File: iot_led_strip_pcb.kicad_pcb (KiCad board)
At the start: 2 copper layers, 50 x 50 mm, 57 parts, among them J1 I2C Expansion, J2 Conn_01x03_Socket, J3 GT-USB-7010ASV, J4 Barrel_Jack_Switch_Pin3Ring, J5 TC2050-IDC_Cortex-M, J6 Conn_01x03_Socket_Solderwire, Q1 BSS138, SW1 RESET, SW2 FLASH, U1 AMS1117-3.3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

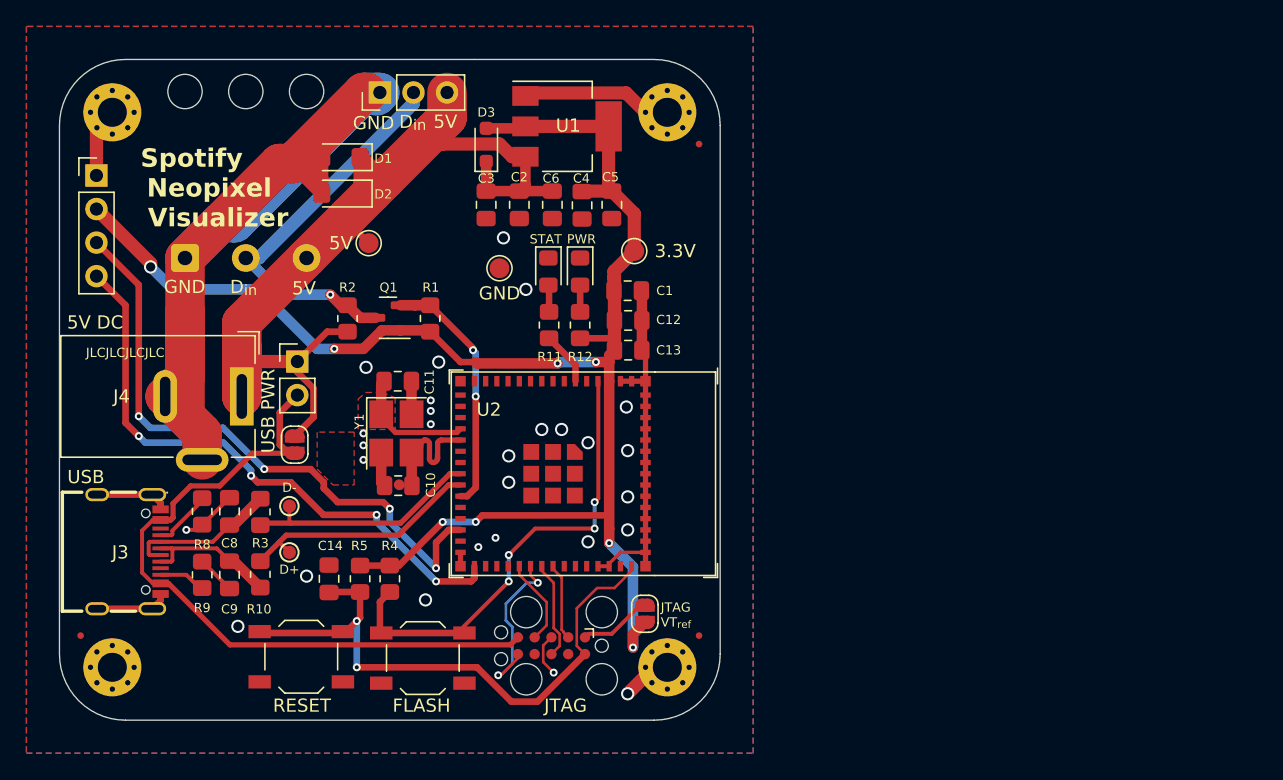
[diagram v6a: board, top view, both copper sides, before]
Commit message: modified sch to change over to esp32-s2-solo-2, should be much easier to solder
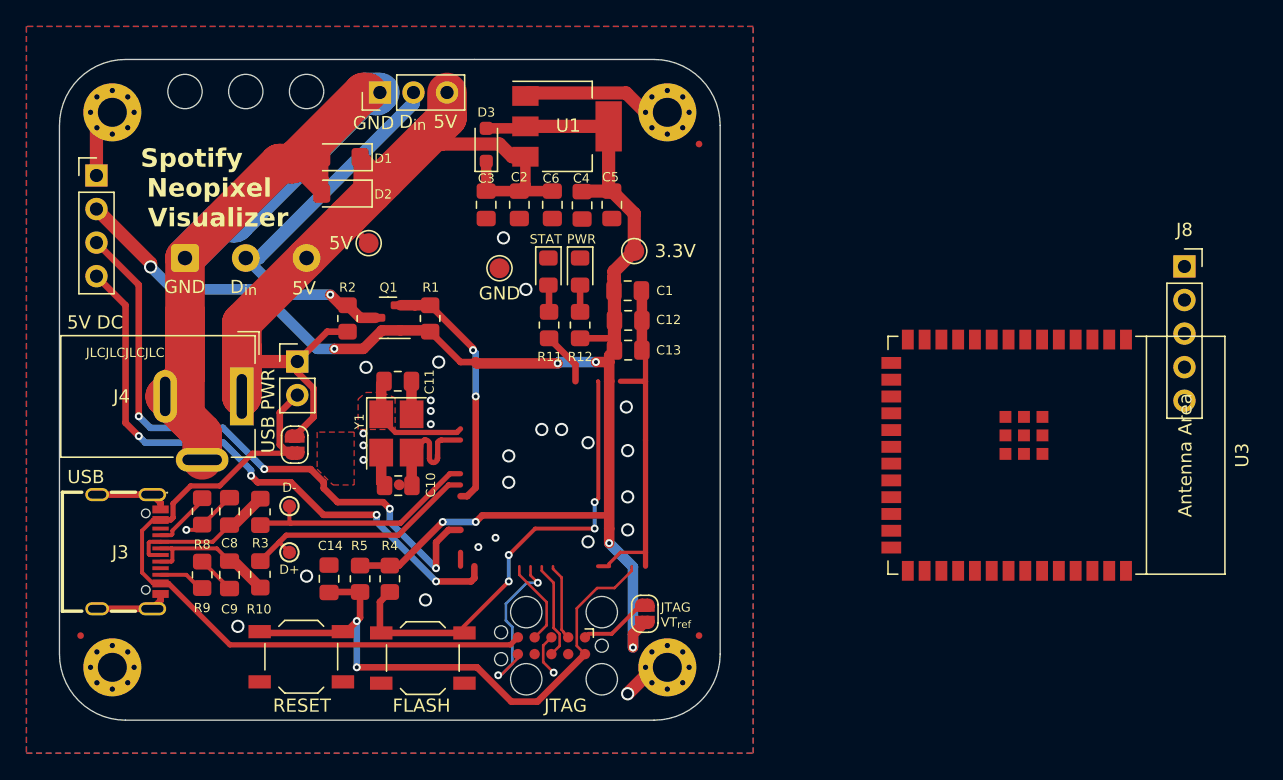
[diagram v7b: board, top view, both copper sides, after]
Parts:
- removed U2: ESP32-S2-MINI-1, PCM_Espressif:ESP32-S2-MINI-1
- added J8: UART, Connector_PinSocket_2.54mm:PinSocket_1x05_P2.54mm_Vertical, F.Cu at (195.1, 85.7)
- added U3: ESP32-S2-SOLO, Espressif:ESP32-S2-SOLO, F.Cu at (182.4, 100.0)
- Y1: value Crystal_32Mhz -> Crystal_32Khz

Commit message: board redesign around ESP32-S2-SOLO-2
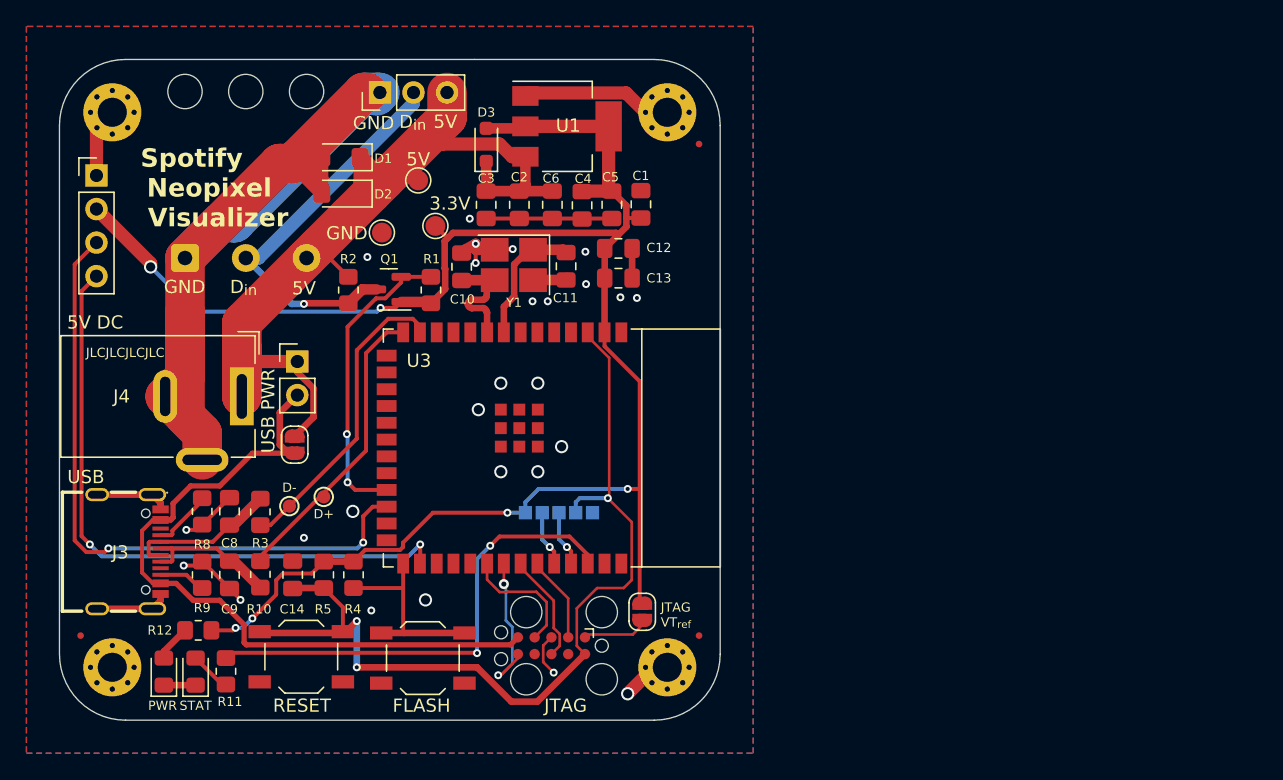
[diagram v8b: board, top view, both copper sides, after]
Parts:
- J8: footprint Connector_PinSocket_2.54mm:PinSocket_1x05_P2.54mm_Vertical -> footprint:5 Pin Pad array; moved to B.Cu
- moved J8 47.7 mm to (151.0, 103.6), turned to 180 degrees
- moved D5 43.7 mm to (117.9, 116.3), turned to 90 degrees
- moved D4 40.4 mm to (120.3, 116.3), turned to 90 degrees
- moved U3 38.2 mm to (144.3, 99.4)
- moved R12 37.0 mm to (120.5, 113.2), turned to 0 degrees
- moved R11 35.8 mm to (122.6, 116.3), turned to 90 degrees
- moved C10 17.2 mm to (140.4, 85.7), turned to 90 degrees
- moved Y1 15.5 mm to (144.4, 85.5), turned to 180 degrees
- moved C11 15.4 mm to (148.3, 85.7), turned to -90 degrees
- moved TP2 15.2 mm to (138.4, 82.6)
- moved TP3 9.30 mm to (134.4, 83.1)
- moved C1 6.61 mm to (154.0, 81.0), turned to 90 degrees
- moved TP1 6.05 mm to (137.2, 79.2)
- moved C12 5.50 mm to (152.3, 84.3)
- moved C13 5.50 mm to (152.3, 86.5)
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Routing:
- net Net-(U3-GPIO2/TOUCH2/ADC1_CH1): track 4.08 -> 36.6 mm, vias 0 -> 2
- net /~{RST}: track 45.0 -> 69.6 mm, vias 2 -> 3
- net BOOT: track 34.9 -> 15.1 mm, vias 4 -> 0
- net +3.3V: track 130.2 -> 138.3 mm, vias 8 -> 6
- net Earth: track 147.0 -> 139.4 mm, vias 28 -> 26
- net /USB_D-: track 18.1 -> 23.2 mm
- net /LV_DIN: track 18.9 -> 23.1 mm
- net /UART_TX: track 0.00 -> 4.23 mm, vias 0 -> 1
- net /UART_RX: track 0.00 -> 4.23 mm, vias 0 -> 1
- net +5V: track 75.4 -> 71.3 mm
- net /USB_D+: track 18.6 -> 22.5 mm
- net /SCL: track 44.9 -> 48.2 mm, vias 4 -> 2
- net /SDA: track 46.8 -> 49.8 mm, vias 4 -> 2
- net /TCK: track 6.61 -> 9.48 mm
- net /TDO: track 13.1 -> 11.6 mm
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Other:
- board text added: "RXD"
- board text added: "TXD"
- board text added: "locked"
- board text added: "~{RST}"
- board text removed: "M2 Mounting Holes"
- board text removed: "Tag-Connect JTAG Header"
